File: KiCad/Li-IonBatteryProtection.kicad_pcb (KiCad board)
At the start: 2 copper layers, 147.2 x 58.3 mm, 81 parts, among them J1 CONN_02X03, J2 CONN_01X02, Q1 IRF540N, Q2 2N2222A, Q3 2N2222A, Q4 2N2222A, Q5 2N2222A, Q6 2N2222A, U1 LM311N, U2 PC817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

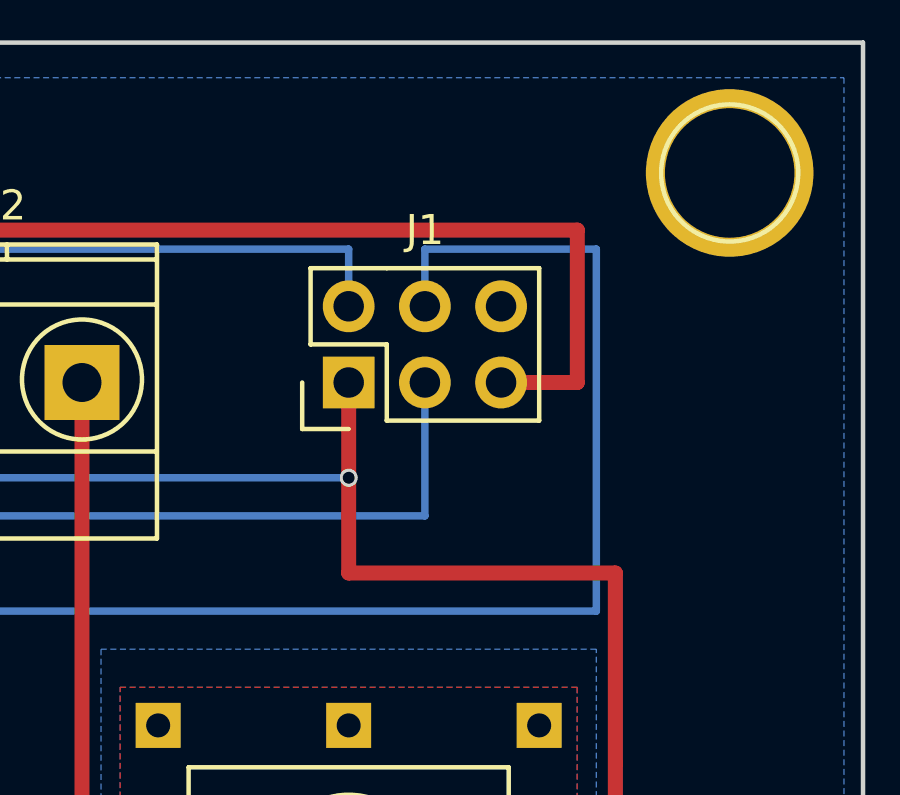
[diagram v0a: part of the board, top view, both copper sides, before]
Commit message: Moved J1 to give more distance between the shroud and the mounting hole.
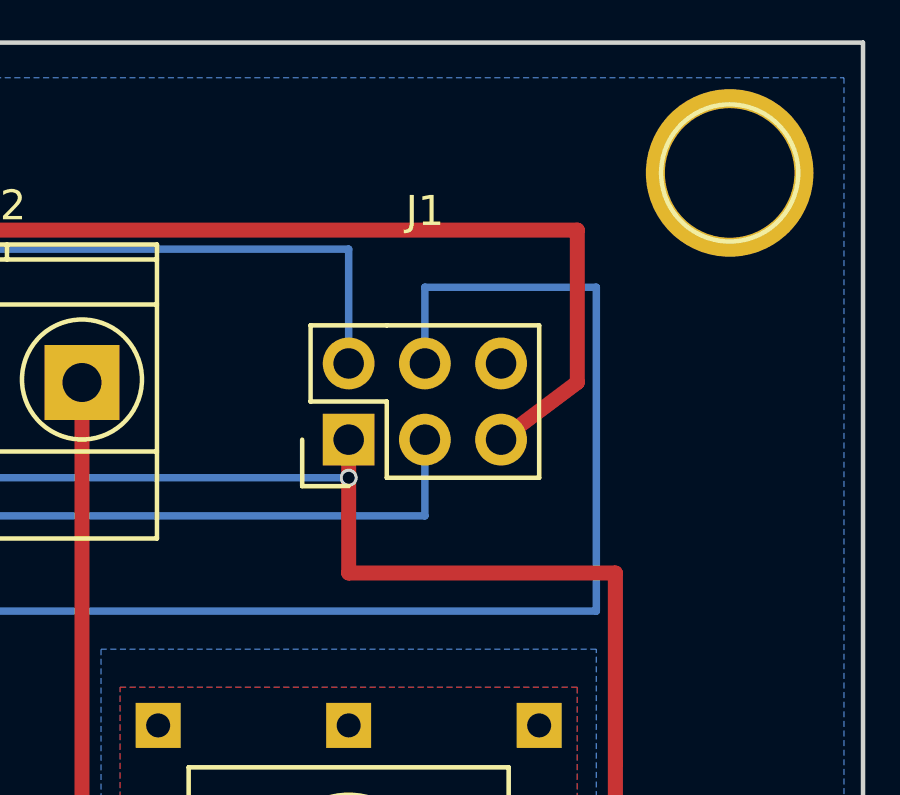
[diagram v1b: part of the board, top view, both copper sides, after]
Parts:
- moved J1 1.91 mm to (190.5, 83.2)
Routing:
- net Battery-2: track 173.5 -> 171.6 mm
- net Battery-1: track 202.5 -> 204.4 mm
- net Battery-GND: track 308.3 -> 306.4 mm
- net Battery-3: track 163.9 -> 163.2 mm
- net Battery-4: track 127.6 -> 128.2 mm
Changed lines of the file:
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@@
   )
   (module Pin_Headers:Pin_Header_Straight_2x03 (layer F.Cu)
-    (at 190.5 81.28 90)
+    (at 190.5 83.185 90)
     (descr "Through hole pin header")
     (tags "pin header")
-    (fp_text reference J1 (at 5.08 2.54 180) (layer F.SilkS)
+    (fp_text reference J1 (at 7.62 2.54 180) (layer F.SilkS)
       (effects (font (size 1 1) (thickness 0.15)))
     )
@@
   (segment (start 70.48754 111.76) (end 70.485 113.665) (width 0.25) (layer F.Cu) (net 2) (status 10))
   (segment (start 70.485 113.665) (end 70.485 115.57) (width 0.25) (layer F.Cu) (net 2) (status 20))
-  (segment (start 190.5 81.28) (end 190.5 84.455) (width 0.5) (layer F.Cu) (net 2) (status 10))
+  (segment (start 190.5 83.185) (end 190.5 84.455) (width 0.5) (layer F.Cu) (net 2) (status 10))
   (segment (start 190.5 84.455) (end 190.5 87.63) (width 0.5) (layer F.Cu) (net 2) (status 10))
   (segment (start 190.5 87.63) (end 199.39 87.63) (width 0.5) (layer F.Cu) (net 2))
@@
   (segment (start 167.64 102.235) (end 166.37 102.235) (width 0.25) (layer B.Cu) (net 6) (status 10))
   (segment (start 176.61 76.2) (end 198.12 76.2) (width 0.5) (layer F.Cu) (net 6))
-  (segment (start 195.58 81.28) (end 198.12 81.28) (width 0.5) (layer F.Cu) (net 6) (status 10))
+  (segment (start 195.58 83.185) (end 198.12 81.28) (width 0.5) (layer F.Cu) (net 6) (status 10))
   (segment (start 198.12 81.28) (end 198.12 76.2) (width 0.5) (layer F.Cu) (net 6))
   (segment (start 176.61 76.2) (end 176.61 81.28) (width 0.5) (layer F.Cu) (net 6) (status 20))
@@
   (segment (start 95.25 115.57) (end 91.44 115.57) (width 0.25) (layer F.Cu) (net 8))
   (segment (start 112.395 88.9) (end 112.395 85.725) (width 0.25) (layer B.Cu) (net 8))
-  (segment (start 190.5 76.835) (end 190.5 78.74) (width 0.25) (layer B.Cu) (net 8))
+  (segment (start 190.5 76.835) (end 190.5 80.645) (width 0.25) (layer B.Cu) (net 8) (status 20))
   (segment (start 114.935 76.835) (end 190.5 76.835) (width 0.25) (layer B.Cu) (net 8))
   (segment (start 114.935 85.725) (end 114.935 76.835) (width 0.25) (layer B.Cu) (net 8))
@@
   (segment (start 120.015 115.57) (end 116.205 115.57) (width 0.25) (layer F.Cu) (net 10))
   (segment (start 137.16 88.9) (end 137.16 86.995) (width 0.25) (layer B.Cu) (net 10))
-  (segment (start 193.04 85.725) (end 193.04 81.28) (width 0.25) (layer B.Cu) (net 10))
+  (segment (start 193.04 85.725) (end 193.04 83.185) (width 0.25) (layer B.Cu) (net 10) (status 20))
   (segment (start 156.21 85.725) (end 193.04 85.725) (width 0.25) (layer B.Cu) (net 10))
   (segment (start 156.21 86.995) (end 156.21 85.725) (width 0.25) (layer B.Cu) (net 10))
@@
   (segment (start 124.46 100.33) (end 124.46 95.25) (width 0.25) (layer F.Cu) (net 12) (status 20))
   (segment (start 130.81 104.775) (end 124.46 100.33) (width 0.25) (layer F.Cu) (net 12))
-  (segment (start 193.04 78.74) (end 193.04 76.835) (width 0.25) (layer B.Cu) (net 12))
-  (segment (start 193.04 76.835) (end 198.755 76.835) (width 0.25) (layer B.Cu) (net 12))
-  (segment (start 198.755 76.835) (end 198.755 88.9) (width 0.25) (layer B.Cu) (net 12))
+  (segment (start 193.04 80.645) (end 193.04 78.105) (width 0.25) (layer B.Cu) (net 12) (status 10))
+  (segment (start 193.04 78.105) (end 198.755 78.105) (width 0.25) (layer B.Cu) (net 12))
+  (segment (start 198.755 78.105) (end 198.755 88.9) (width 0.25) (layer B.Cu) (net 12))
   (segment (start 198.755 88.9) (end 164.465 88.9) (width 0.25) (layer B.Cu) (net 12))
   (via (at 164.465 88.9) (size 0.6) (drill 0.4) (layers F.Cu B.Cu) (net 12))
@@
   (segment (start 156.845 116.205) (end 161.925 114.3) (width 0.25) (layer F.Cu) (net 12) (status 20))
   (segment (start 161.925 88.9) (end 164.465 88.9) (width 0.25) (layer F.Cu) (net 12) (status 10))
-  (segment (start 193.04 78.74) (end 193.04 78.74) (width 0.25) (layer B.Cu) (net 12) (status 30))
+  (segment (start 193.04 80.645) (end 193.04 80.645) (width 0.25) (layer B.Cu) (net 12) (status 30))
   (segment (start 144.78 115.57) (end 147.32 118.11) (width 0.25) (layer F.Cu) (net 12) (status 30))
   (segment (start 137.16 109.22) (end 145.415 111.76254) (width 0.25) (layer B.Cu) (net 12) (status 10))
